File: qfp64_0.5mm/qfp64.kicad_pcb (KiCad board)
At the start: 2 copper layers, 21.6 x 21.6 mm, 1 part

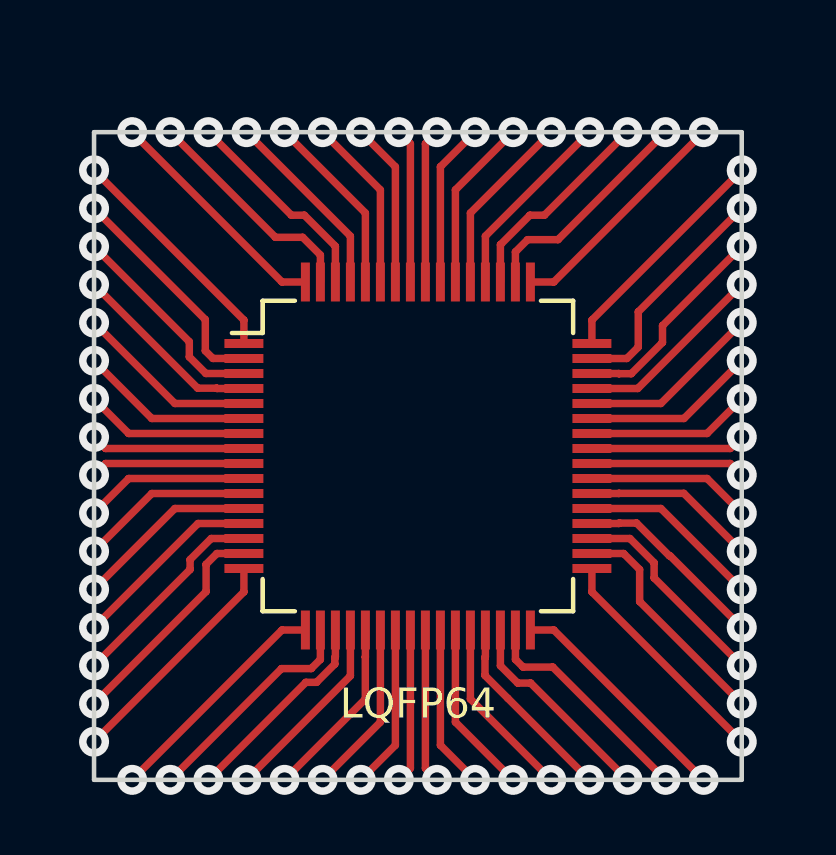
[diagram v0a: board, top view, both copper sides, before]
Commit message: Updating QFP64 footprint to allow more space at its corners.
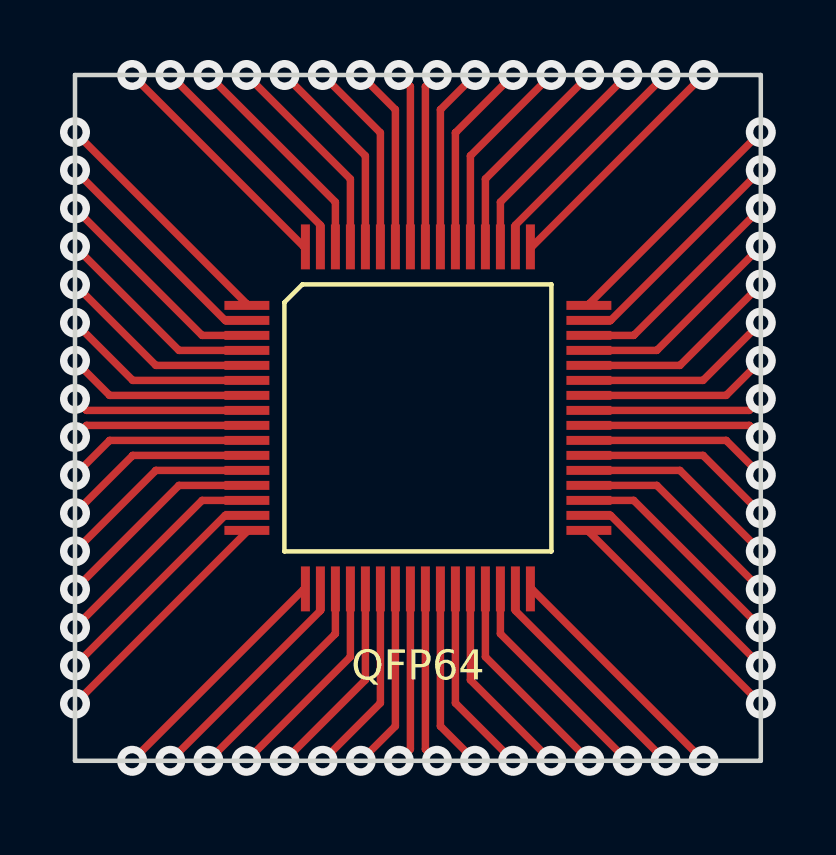
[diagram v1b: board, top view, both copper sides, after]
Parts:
- removed ?: LQFP64, apexelectrix/Apex.pretty:LQFP-64_10x10mm_Pitch0.5mm
- added REF**: QFP64, adamgreig/agg-kicad/agg.pretty:LQFP-64, F.Cu at (139.1, 76.8)
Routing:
- net (no net): track 414.1 -> 448.6 mm
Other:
- board size 21.6 x 21.6 mm -> 22.9 x 22.9 mm
- net class Default: clearance 0.2 -> 0.4; via_dia 0.8 -> 1; via_drill 0.4 -> 0.5
- rule trace_clearance: 0.2 -> 0.4
- board text added: "Castellated LQFP64 Breakout (v2) @coddingtonbear 20 December 2017 0.5mm Pitch"
- board text removed: "Castellated LQFP64 Breakout @coddingtonbear 22 Nov 2017"

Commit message: Fixing track spacing problem found by u/piranha on reddit.  Fixes #1.
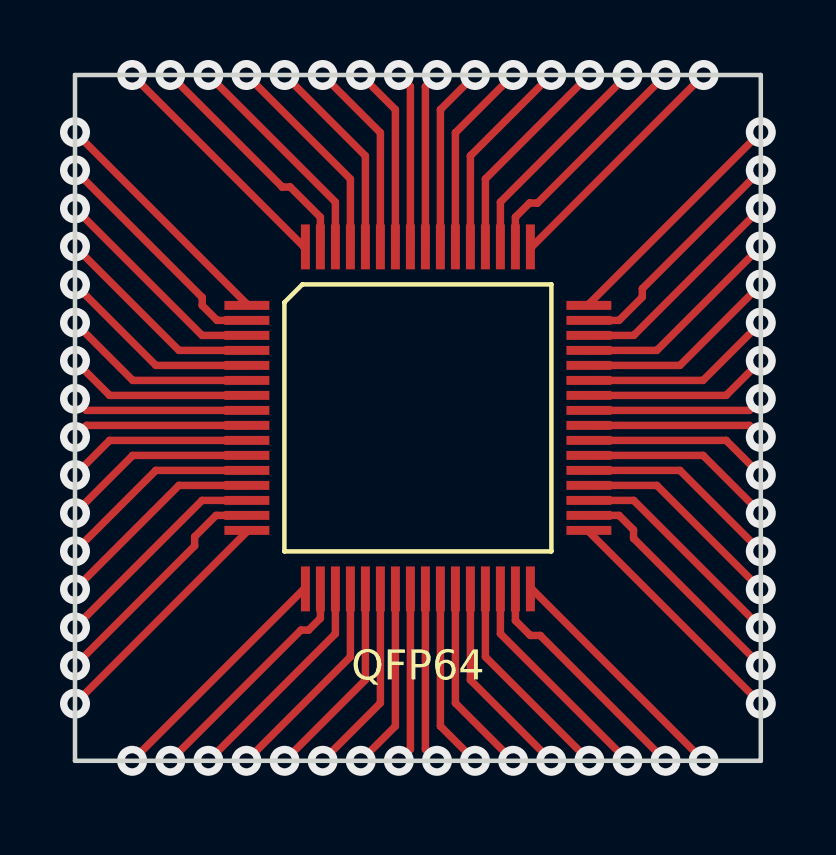
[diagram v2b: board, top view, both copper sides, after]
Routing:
- net (no net): track 448.6 -> 455.7 mm
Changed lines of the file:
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@@
     (thickness 1.6)
     (drawings 5)
-    (tracks 192)
+    (tracks 216)
     (zones 0)
     (modules 1)
@@
     (effects (font (size 0.75 0.75) (thickness 0.1875)) (justify left mirror))
   )
+  (segment (start 131.8768 73.0885) (end 131.8768 72.8218) (width 0.25) (layer F.Cu) (net 0))
+  (segment (start 131.8768 72.8218) (end 127.635 68.58) (width 0.25) (layer F.Cu) (net 0))
+  (segment (start 132.3733 73.585) (end 131.8768 73.0885) (width 0.25) (layer F.Cu) (net 0))
+  (segment (start 133.365 73.585) (end 132.3733 73.585) (width 0.25) (layer F.Cu) (net 0))
+  (segment (start 131.6228 80.7974) (end 131.6228 81.1022) (width 0.25) (layer F.Cu) (net 0))
+  (segment (start 131.6228 81.1022) (end 127.635 85.09) (width 0.25) (layer F.Cu) (net 0))
+  (segment (start 132.3352 80.085) (end 131.6228 80.7974) (width 0.25) (layer F.Cu) (net 0))
+  (segment (start 133.365 80.085) (end 132.3352 80.085) (width 0.25) (layer F.Cu) (net 0))
+  (segment (start 135.4201 83.9089) (end 135.1661 83.9089) (width 0.25) (layer F.Cu) (net 0))
+  (segment (start 135.1661 83.9089) (end 130.81 88.265) (width 0.25) (layer F.Cu) (net 0))
+  (segment (start 135.815 83.514) (end 135.4201 83.9089) (width 0.25) (layer F.Cu) (net 0))
+  (segment (start 135.815 82.535) (end 135.815 83.514) (width 0.25) (layer F.Cu) (net 0))
+  (segment (start 142.8115 84.0867) (end 143.1417 84.0867) (width 0.25) (layer F.Cu) (net 0))
+  (segment (start 143.1417 84.0867) (end 147.32 88.265) (width 0.25) (layer F.Cu) (net 0))
+  (segment (start 142.315 83.5902) (end 142.8115 84.0867) (width 0.25) (layer F.Cu) (net 0))
+  (segment (start 142.315 82.535) (end 142.315 83.5902) (width 0.25) (layer F.Cu) (net 0))
+  (segment (start 146.2532 80.5688) (end 146.2532 80.8482) (width 0.25) (layer F.Cu) (net 0))
+  (segment (start 146.2532 80.8482) (end 150.495 85.09) (width 0.25) (layer F.Cu) (net 0))
+  (segment (start 145.7694 80.085) (end 146.2532 80.5688) (width 0.25) (layer F.Cu) (net 0))
+  (segment (start 144.765 80.085) (end 145.7694 80.085) (width 0.25) (layer F.Cu) (net 0))
+  (segment (start 146.5453 72.8091) (end 146.5453 72.5297) (width 0.25) (layer F.Cu) (net 0))
+  (segment (start 146.5453 72.5297) (end 150.495 68.58) (width 0.25) (layer F.Cu) (net 0))
+  (segment (start 145.7694 73.585) (end 146.5453 72.8091) (width 0.25) (layer F.Cu) (net 0))
+  (segment (start 144.765 73.585) (end 145.7694 73.585) (width 0.25) (layer F.Cu) (net 0))
+  (segment (start 142.7861 69.6722) (end 143.0528 69.6722) (width 0.25) (layer F.Cu) (net 0))
+  (segment (start 143.0528 69.6722) (end 147.32 65.405) (width 0.25) (layer F.Cu) (net 0))
+  (segment (start 142.315 70.1433) (end 142.7861 69.6722) (width 0.25) (layer F.Cu) (net 0))
+  (segment (start 142.315 71.135) (end 142.315 70.1433) (width 0.25) (layer F.Cu) (net 0))
+  (segment (start 134.8105 69.1388) (end 134.5438 69.1388) (width 0.25) (layer F.Cu) (net 0))
+  (segment (start 134.5438 69.1388) (end 130.81 65.405) (width 0.25) (layer F.Cu) (net 0))
+  (segment (start 135.815 70.1433) (end 134.8105 69.1388) (width 0.25) (layer F.Cu) (net 0))
+  (segment (start 135.815 71.135) (end 135.815 70.1433) (width 0.25) (layer F.Cu) (net 0))
   (segment (start 133.365 73.085) (end 133.365 73.04) (width 0.25) (layer F.Cu) (net 0))
   (segment (start 133.365 73.04) (end 127.635 67.31) (width 0.25) (layer F.Cu) (net 0))
   (segment (start 133.365 73.585) (end 132.64 73.585) (width 0.25) (layer F.Cu) (net 0))
-  (segment (start 132.64 73.585) (end 127.635 68.58) (width 0.25) (layer F.Cu) (net 0))
   (segment (start 133.365 74.085) (end 131.87 74.085) (width 0.25) (layer F.Cu) (net 0))
   (segment (start 131.87 74.085) (end 127.635 69.85) (width 0.25) (layer F.Cu) (net 0))
@@
   (segment (start 133.365 80.63) (end 127.635 86.36) (width 0.25) (layer F.Cu) (net 0))
   (segment (start 133.365 80.085) (end 132.64 80.085) (width 0.25) (layer F.Cu) (net 0))
-  (segment (start 132.64 80.085) (end 127.635 85.09) (width 0.25) (layer F.Cu) (net 0))
   (segment (start 133.365 79.585) (end 131.87 79.585) (width 0.25) (layer F.Cu) (net 0))
   (segment (start 131.87 79.585) (end 127.635 83.82) (width 0.25) (layer F.Cu) (net 0))
@@
   (segment (start 142.86 82.535) (end 148.59 88.265) (width 0.25) (layer F.Cu) (net 0))
   (segment (start 142.315 82.535) (end 142.315 83.26) (width 0.25) (layer F.Cu) (net 0))
-  (segment (start 142.315 83.26) (end 147.32 88.265) (width 0.25) (layer F.Cu) (net 0))
   (segment (start 141.815 82.535) (end 141.815 84.03) (width 0.25) (layer F.Cu) (net 0))
   (segment (start 141.815 84.03) (end 146.05 88.265) (width 0.25) (layer F.Cu) (net 0))
@@
   (segment (start 135.27 82.535) (end 129.54 88.265) (width 0.25) (layer F.Cu) (net 0))
   (segment (start 135.815 82.535) (end 135.815 83.26) (width 0.25) (layer F.Cu) (net 0))
-  (segment (start 135.815 83.26) (end 130.81 88.265) (width 0.25) (layer F.Cu) (net 0))
   (segment (start 136.315 82.535) (end 136.315 84.03) (width 0.25) (layer F.Cu) (net 0))
   (segment (start 136.315 84.03) (end 132.08 88.265) (width 0.25) (layer F.Cu) (net 0))
@@
   (segment (start 144.765 80.63) (end 150.495 86.36) (width 0.25) (layer F.Cu) (net 0))
   (segment (start 144.765 80.085) (end 145.49 80.085) (width 0.25) (layer F.Cu) (net 0))
-  (segment (start 145.49 80.085) (end 150.495 85.09) (width 0.25) (layer F.Cu) (net 0))
   (segment (start 144.765 79.585) (end 146.26 79.585) (width 0.25) (layer F.Cu) (net 0))
   (segment (start 146.26 79.585) (end 150.495 83.82) (width 0.25) (layer F.Cu) (net 0))
@@
   (segment (start 144.765 73.04) (end 150.495 67.31) (width 0.25) (layer F.Cu) (net 0))
   (segment (start 144.765 73.585) (end 145.49 73.585) (width 0.25) (layer F.Cu) (net 0))
-  (segment (start 145.49 73.585) (end 150.495 68.58) (width 0.25) (layer F.Cu) (net 0))
   (segment (start 144.765 74.085) (end 146.26 74.085) (width 0.25) (layer F.Cu) (net 0))
   (segment (start 146.26 74.085) (end 150.495 69.85) (width 0.25) (layer F.Cu) (net 0))
@@
   (segment (start 142.86 71.135) (end 148.59 65.405) (width 0.25) (layer F.Cu) (net 0))
   (segment (start 142.315 71.135) (end 142.315 70.41) (width 0.25) (layer F.Cu) (net 0))
-  (segment (start 142.315 70.41) (end 147.32 65.405) (width 0.25) (layer F.Cu) (net 0))
   (segment (start 141.815 71.135) (end 141.815 69.64) (width 0.25) (layer F.Cu) (net 0))
   (segment (start 141.815 69.64) (end 146.05 65.405) (width 0.25) (layer F.Cu) (net 0))
@@
   (segment (start 135.27 71.135) (end 129.54 65.405) (width 0.25) (layer F.Cu) (net 0))
   (segment (start 135.815 71.135) (end 135.815 70.41) (width 0.25) (layer F.Cu) (net 0))
-  (segment (start 135.815 70.41) (end 130.81 65.405) (width 0.25) (layer F.Cu) (net 0))
+  (via (at 130.81 65.405) (size 1) (drill 0.5) (layers F.Cu B.Cu) (net 0))
   (segment (start 136.315 71.135) (end 136.315 69.64) (width 0.25) (layer F.Cu) (net 0))
   (segment (start 136.315 69.64) (end 132.08 65.405) (width 0.25) (layer F.Cu) (net 0))
@@
   (segment (start 138.815 71.135) (end 138.815 65.79) (width 0.25) (layer F.Cu) (net 0))
   (segment (start 138.815 65.79) (end 138.43 65.405) (width 0.25) (layer F.Cu) (net 0))
-  (via (at 130.81 65.405) (size 1) (drill 0.5) (layers F.Cu B.Cu) (net 0))
   (via (at 127.635 67.31) (size 1) (drill 0.5) (layers F.Cu B.Cu) (net 0))
   (via (at 127.635 68.58) (size 1) (drill 0.5) (layers F.Cu B.Cu) (net 0))
